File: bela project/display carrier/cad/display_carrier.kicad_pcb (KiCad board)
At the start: 2 copper layers, 194.1 x 89.3 mm, 11 parts, among them U1 PocketBeagle2

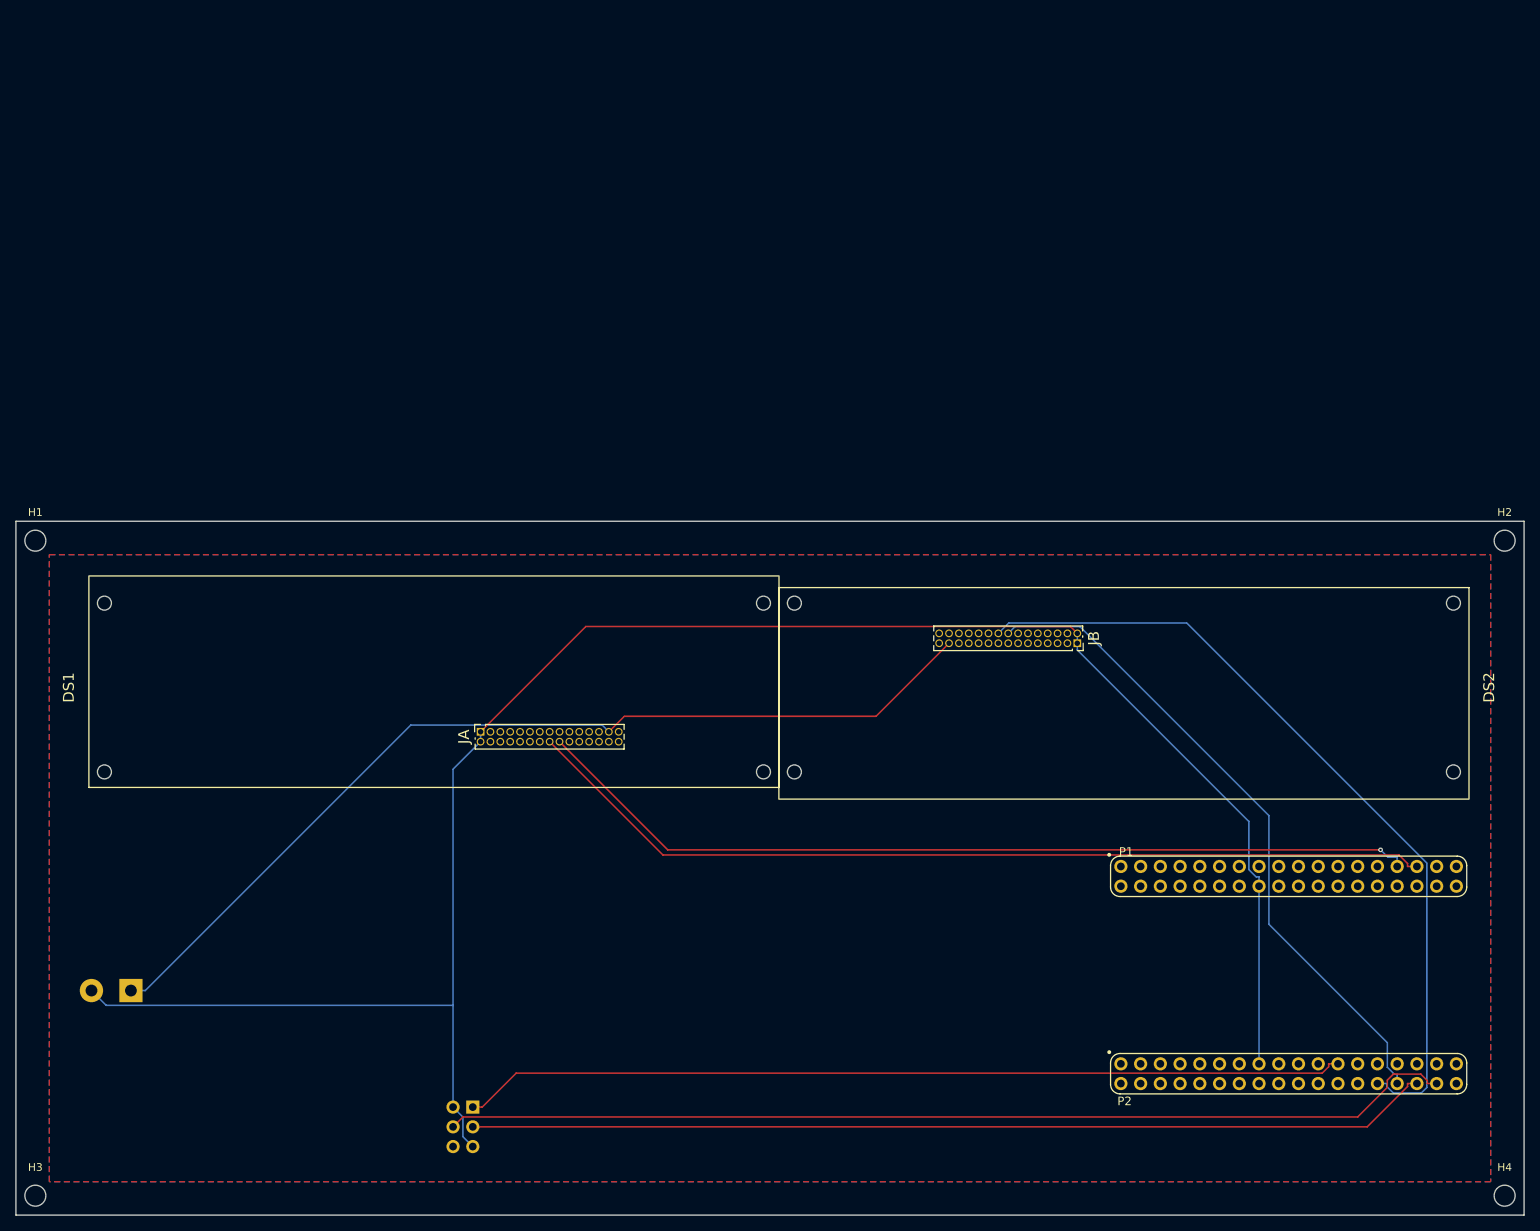
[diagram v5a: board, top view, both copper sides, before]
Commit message: display carrier: 12-encoder faceplate + RP2040 reader (placed) + book Ch.03
Faceplate: 12 Bourns PEC12R-4020F-S0024 endless no-detent encoders (3 per
screen, on the active-area thirds, Digitakt/Push style), parameterised in
gen_carrier to the hand-placed reference — placing the SHAFT (not the pad-A
origin, offset by the +7.5,2.5 bushing) on each icon centre. Generated an
encoder 3D-model approximation (Rotary_Encoder.3dshapes is empty here) and
fixed its offset for KiCad's 3D-viewer Y-flip. Screen model widened to the
real 82.56mm active area (fuller black for alignment viewing). Connectors
relegated to a bottom skirt to clear the knobs.

RP2040 encoder-reader subsystem placed on the back skirt (MCU + QSPI flash +
12MHz xtal + 3V3 LDO + 2x 74HC165 + USB-C). Pin-map DATASHEET-VERIFIED (KiCad
MCU_RaspberryPi symbol + RP2040 datasheet): GPIO0-23 -> 12 enc A/B, GPIO24/25
-> I2C to the Beagle, GPIO26-28 -> the shift-register switch scan (29/30 GPIO).
Wiring/routing is the next step. New footprints in lib.pretty.

Book: Chapter 03 "The faceplate - twelve knobs and a brain" (the RP2040 why +
2 Blender faceplate renders) and a real LILYGO product photo; AMOLED->TFT fix.

Co-Authored-By: Claude Opus 4.8 (1M context) <noreply@anthropic.com>
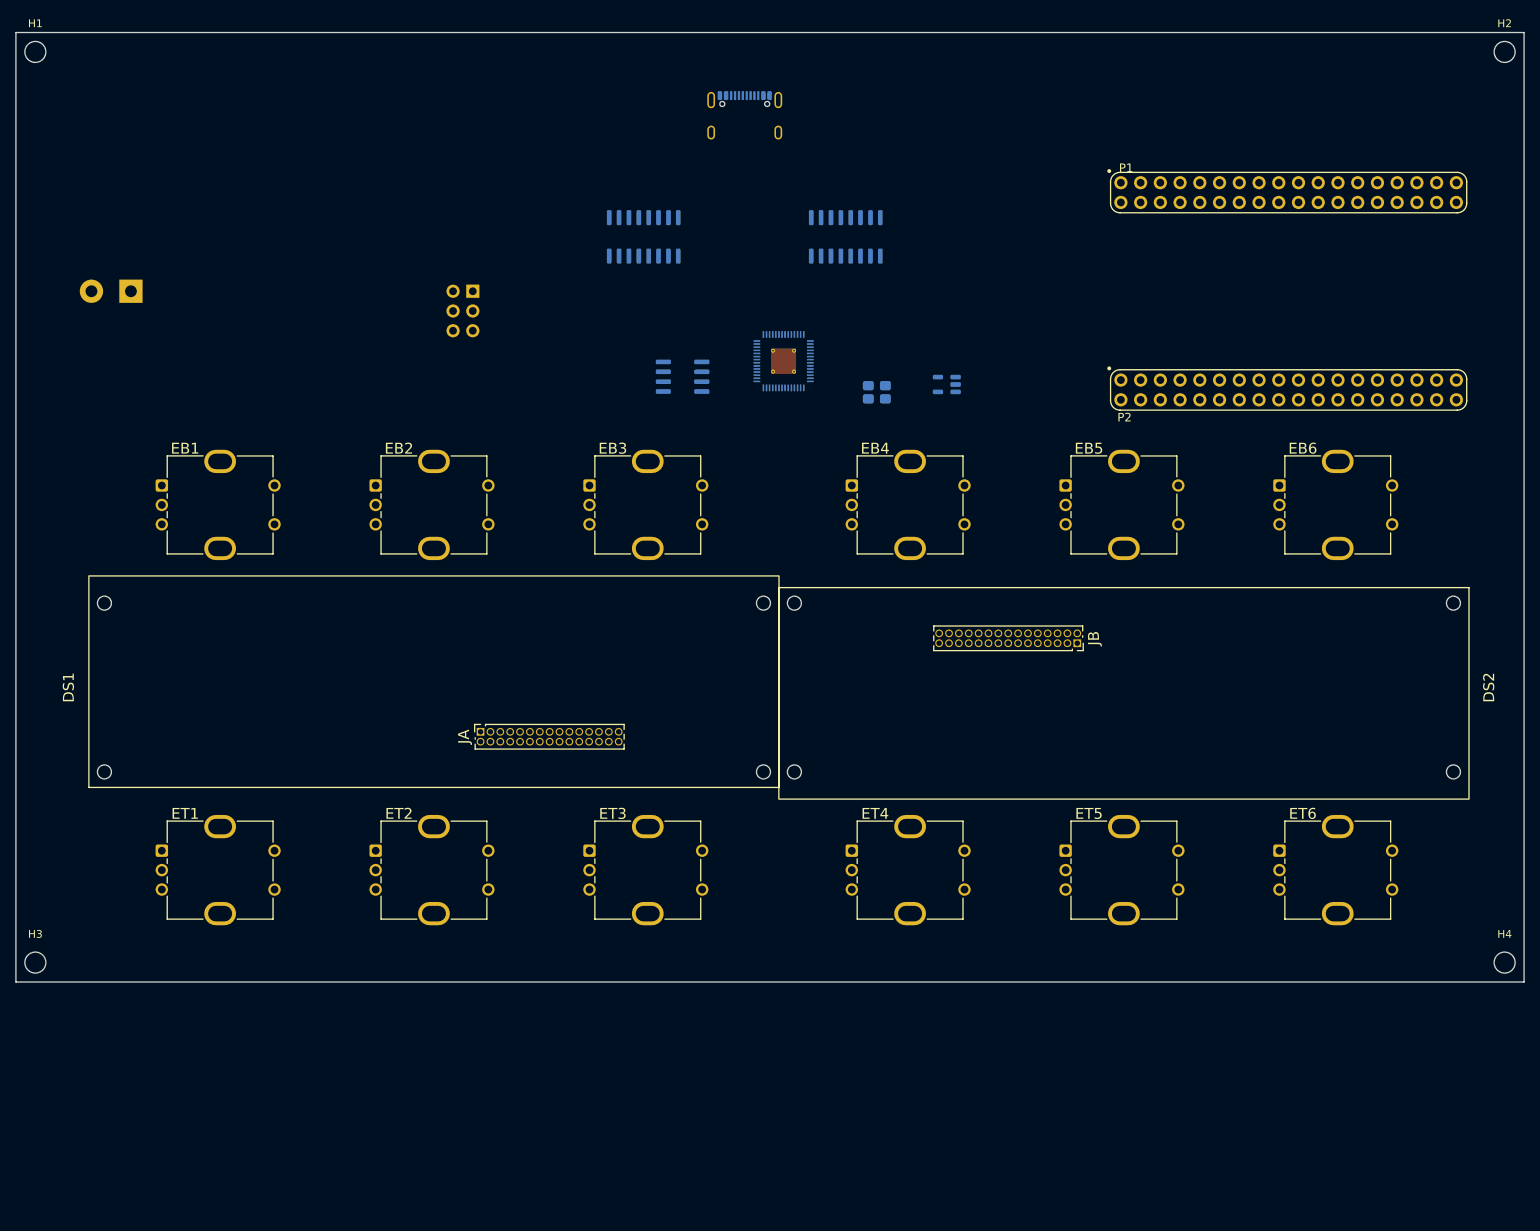
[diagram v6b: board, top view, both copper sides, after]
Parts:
- added EB1: ENC, RotaryEncoder_PEC12R_Vertical, F.Cu at (20.0, -1.00)
- added EB2: ENC, RotaryEncoder_PEC12R_Vertical, F.Cu at (47.5, -1.00)
- added EB3: ENC, RotaryEncoder_PEC12R_Vertical, F.Cu at (75.0, -1.00)
- added EB4: ENC, RotaryEncoder_PEC12R_Vertical, F.Cu at (108.8, -1.00)
- added EB5: ENC, RotaryEncoder_PEC12R_Vertical, F.Cu at (136.3, -1.00)
- added EB6: ENC, RotaryEncoder_PEC12R_Vertical, F.Cu at (163.8, -1.00)
- added ET1: ENC, RotaryEncoder_PEC12R_Vertical, F.Cu at (20.0, 46.0)
- added ET2: ENC, RotaryEncoder_PEC12R_Vertical, F.Cu at (47.5, 46.0)
- added ET3: ENC, RotaryEncoder_PEC12R_Vertical, F.Cu at (75.0, 46.0)
- added ET4: ENC, RotaryEncoder_PEC12R_Vertical, F.Cu at (108.8, 46.0)
- added ET5: ENC, RotaryEncoder_PEC12R_Vertical, F.Cu at (136.3, 46.0)
- added ET6: ENC, RotaryEncoder_PEC12R_Vertical, F.Cu at (163.8, 46.0)
- added J_USB: USB, USBC, B.Cu at (95.0, -47.5)
- added U2: RP2040, RP2040_QFN56, B.Cu at (100.0, -17.0)
- added U3: W25Q128, Flash_SOIC8, B.Cu at (87.0, -15.0)
- added U4: 3V3, LDO_SOT235, B.Cu at (121.0, -14.0)
- added U5: 74HC165, SR_74HC165_SOIC16, B.Cu at (82.0, -33.0)
- added U6: 74HC165, SR_74HC165_SOIC16, B.Cu at (108.0, -33.0)
- added Y1: 12MHz, XTAL_3225, B.Cu at (112.0, -13.0)
- moved J_MIDI 105.0 mm to (60.0, -26.0)
- moved J_PWR 90.0 mm to (16.0, -26.0)
- moved U1 88.0 mm to (165.0, -26.0)
- moved H1 62.9 mm to (3.70, -56.8)
- moved H2 62.9 mm to (192.8, -56.8)
- moved H3 30.0 mm to (3.70, 60.4)
- moved H4 30.0 mm to (192.8, 60.4)
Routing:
- net GND: track 251.3 -> 0.00 mm
- net MIDI_TX: track 130.7 -> 0.00 mm
- net +5V: track 124.5 -> 0.00 mm
- net MIDI_RX: track 124.0 -> 0.00 mm
- net DA_RX: track 118.5 -> 0.00 mm
- net DA_TX: track 115.2 -> 0.00 mm, vias 1 -> 0
- net +3V3: track 113.9 -> 0.00 mm
- net DB_TX: track 104.7 -> 0.00 mm
- net DB_RX: track 85.5 -> 0.00 mm
- removed copper zone on B.Cu, net GND
- removed copper zone on F.Cu, net GND
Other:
- board size 194.1 x 89.3 mm -> 194.1 x 122.2 mm
